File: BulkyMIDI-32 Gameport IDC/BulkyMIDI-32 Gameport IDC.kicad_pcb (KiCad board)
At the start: 2 copper layers, 41.4 x 53 mm, 12 parts, among them J1 Gameport, J2 MIDI OUT, J3 MIDI IN, U1 6N138, U3 74LS00

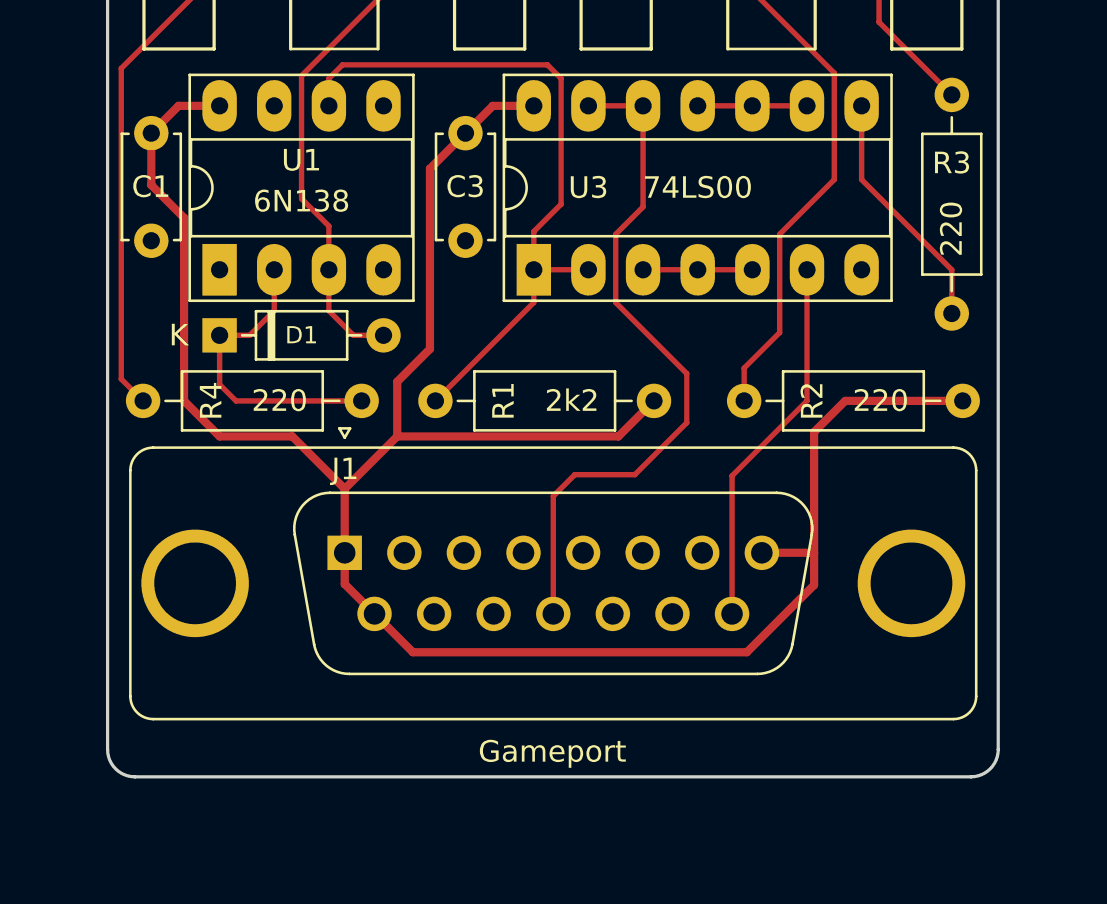
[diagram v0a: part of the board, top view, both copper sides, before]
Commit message: Gameport adapter (IDC connector)
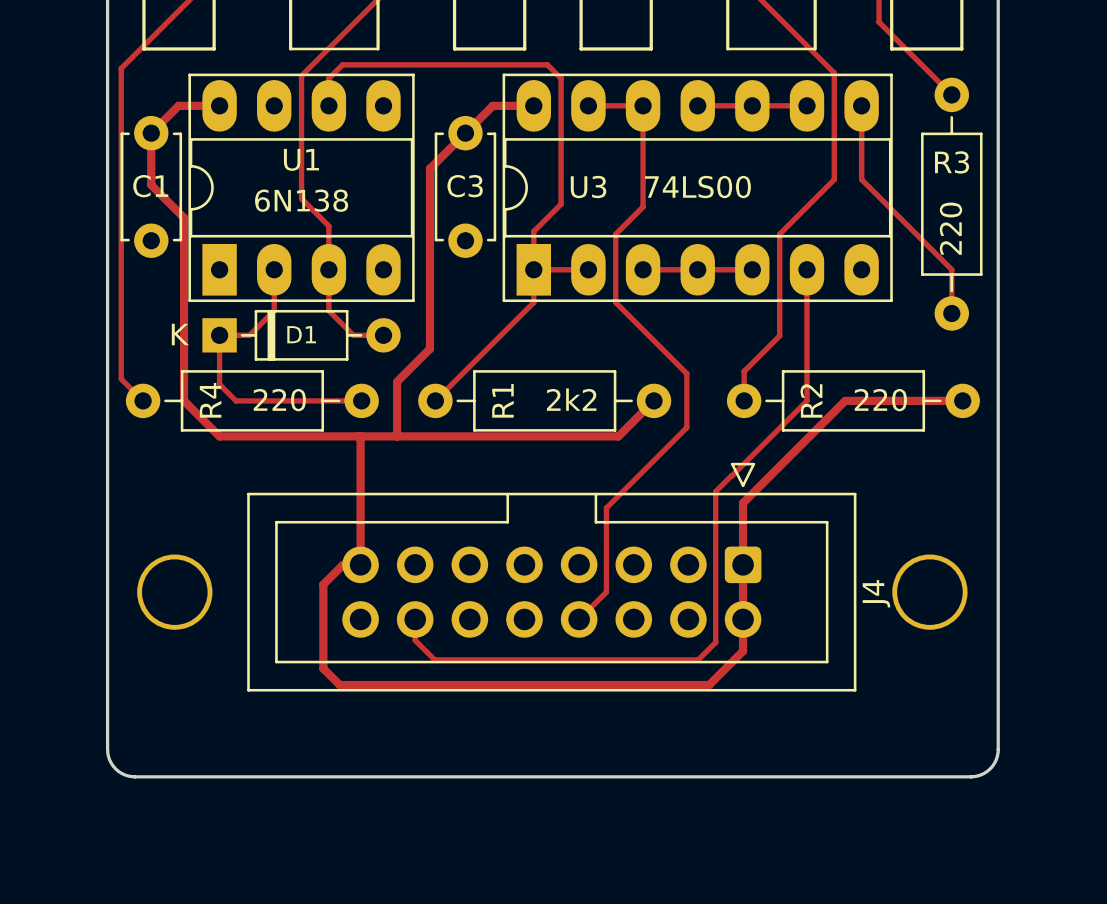
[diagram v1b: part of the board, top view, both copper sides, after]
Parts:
- removed J1: Gameport, RND_DSUB:DSUB-15_Male_Vertical_Pitch2.77x2.84mm
- added J4: Gameport, Gameport:Gameport_IDC, F.Cu at (126.9, 110.2)
- added M1: Mounting, mounting:M3, F.Cu at (100.5, 111.5)
- added M2: Mounting, mounting:M3, F.Cu at (135.6, 111.5)
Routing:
- net MIDI_RxD: track 17.4 -> 34.7 mm
- net +5V: track 107.0 -> 110.7 mm
- net MIDI_TxD: track 32.3 -> 30.4 mm
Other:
- board text added: "BulkyMIDI-32 Gameport IDC (rev. A) github.com/tebl"
- board text removed: "BulkyMIDI-32 Gameport (rev. A) github.com/tebl"
